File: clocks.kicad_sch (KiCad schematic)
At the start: 1 part, among them U10 Si5351C-B-GM

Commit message: Minor updates
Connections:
- net GND: now reaches U10.21 (GND)
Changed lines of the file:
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@@
 	(paper "A4")
 	(symbol
-		(lib_id "Oscillator:Si5351C-B-GM")
-		(at 85.09 87.63 0)
+		(lib_id "power:GND")
+		(at 115.57 92.71 0)
 		(unit 1)
 		(exclude_from_sim no)
@@
 		(on_board yes)
 		(dnp no)
+		(fields_autoplaced yes)
+		(property "Reference" "#PWR058"
+			(at 115.57 99.06 0)
+			(effects
+				(font
+					(size 1.27 1.27)
+				)
+				(hide yes)
+			)
+		)
+		(property "Value" "GND"
+			(at 115.57 97.79 0)
+			(effects
+				(font
+					(size 1.27 1.27)
+				)
+			)
+		)
+		(property "Footprint" ""
+			(at 115.57 92.71 0)
+			(effects
+				(font
+					(size 1.27 1.27)
+				)
+				(hide yes)
+			)
+		)
+		(property "Datasheet" ""
+			(at 115.57 92.71 0)
+			(effects
+				(font
+					(size 1.27 1.27)
+				)
+				(hide yes)
+			)
+		)
+		(property "Description" "Power symbol creates a global label with name \"GND\" , ground"
+			(at 115.57 92.71 0)
+			(effects
+				(font
+					(size 1.27 1.27)
+				)
+				(hide yes)
+			)
+		)
+		(pin "1"
+		)
+		(instances
+			(project ""
+				(path "/b16dfd04-6bfc-4d2d-ba2c-9a843d57dfb1/bef03a1a-2df5-41e5-bcca-109c5f92fdce"
+					(reference "#PWR058")
+					(unit 1)
+				)
+			)
+		)
+	)
+	(symbol
+		(lib_id "Oscillator:Si5351C-B-GM")
+		(at 115.57 69.85 0)
+		(unit 1)
+		(exclude_from_sim no)
+		(in_bom yes)
+		(on_board yes)
+		(dnp no)
+		(fields_autoplaced yes)
 		(property "Reference" "U10"
-			(at 87.2841 110.49 0)
+			(at 117.7641 92.71 0)
 			(effects
 				(font
@@
 		)
 		(property "Value" "Si5351C-B-GM"
-			(at 87.2841 113.03 0)
+			(at 117.7641 95.25 0)
 			(effects
 				(font
@@
 		)
 		(property "Footprint" "Package_DFN_QFN:QFN-20-1EP_4x4mm_P0.5mm_EP2.7x2.7mm"
-			(at 85.09 118.11 0)
+			(at 115.57 100.33 0)
 			(effects
 				(font
@@
 		)
 		(property "Datasheet" "https://www.silabs.com/documents/public/data-sheets/Si5351-B.pdf"
-			(at 85.09 87.63 0)
+			(at 115.57 69.85 0)
 			(effects
 				(font
@@
 		)
 		(property "Description" "I2C Programmable Any-Frequency CMOS Clock Generator, QFN-20"
-			(at 85.09 87.63 0)
+			(at 115.57 69.85 0)
 			(effects
 				(font
@@
 			)
 		)
-		(pin "2"
-		)
-		(pin "21"
-		)
-		(pin "8"
-		)
-		(pin "10"
-		)
-		(pin "1"
-		)
-		(pin "18"
-		)
-		(pin "19"
-		)
-		(pin "11"
-		)
-		(pin "17"
-		)
-		(pin "16"
+		(pin "20"
 		)
 		(pin "9"
@@
 		(pin "12"
 		)
+		(pin "18"
+		)
+		(pin "14"
+		)
+		(pin "16"
+		)
 		(pin "3"
+		)
+		(pin "15"
+		)
+		(pin "17"
+		)
+		(pin "4"
+		)
+		(pin "2"
+		)
+		(pin "10"
+		)
+		(pin "7"
+		)
+		(pin "19"
+		)
+		(pin "8"
+		)
+		(pin "21"
+		)
+		(pin "6"
+		)
+		(pin "1"
+		)
+		(pin "11"
+		)
+		(pin "13"
 		)
 		(pin "5"
 		)
-		(pin "4"
-		)
-		(pin "7"
-		)
-		(pin "6"
-		)
-		(pin "14"
-		)
-		(pin "15"
-		)
-		(pin "20"
-		)
-		(pin "13"
-		)
 		(instances
-			(project "albert"
+			(project ""
 				(path "/b16dfd04-6bfc-4d2d-ba2c-9a843d57dfb1/bef03a1a-2df5-41e5-bcca-109c5f92fdce"
 					(reference "U10")

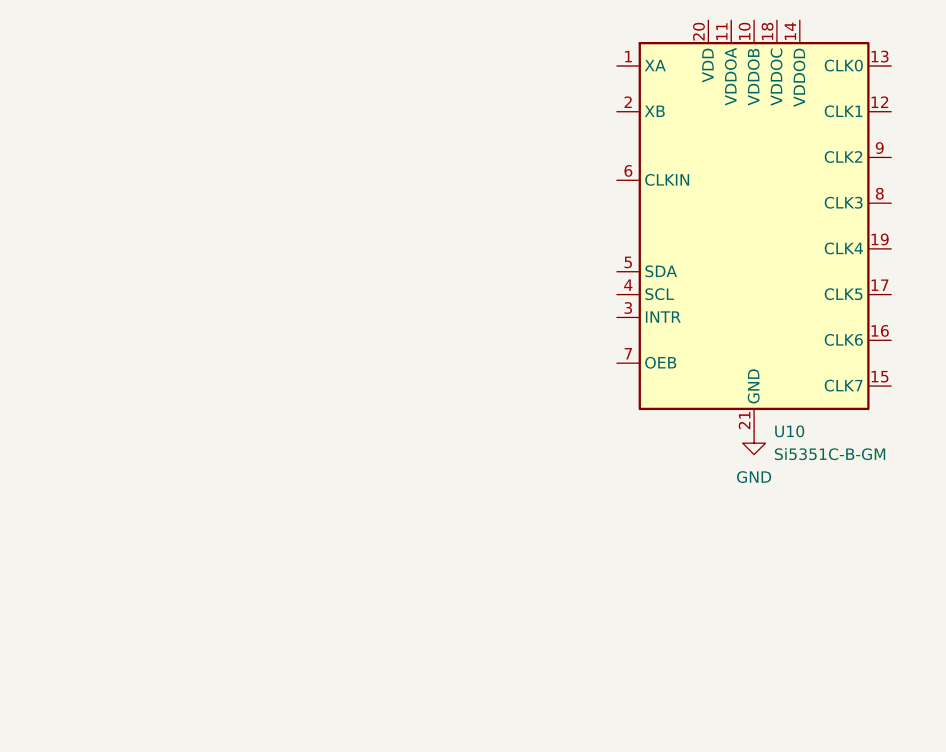
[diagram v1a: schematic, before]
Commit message: Added pMCU
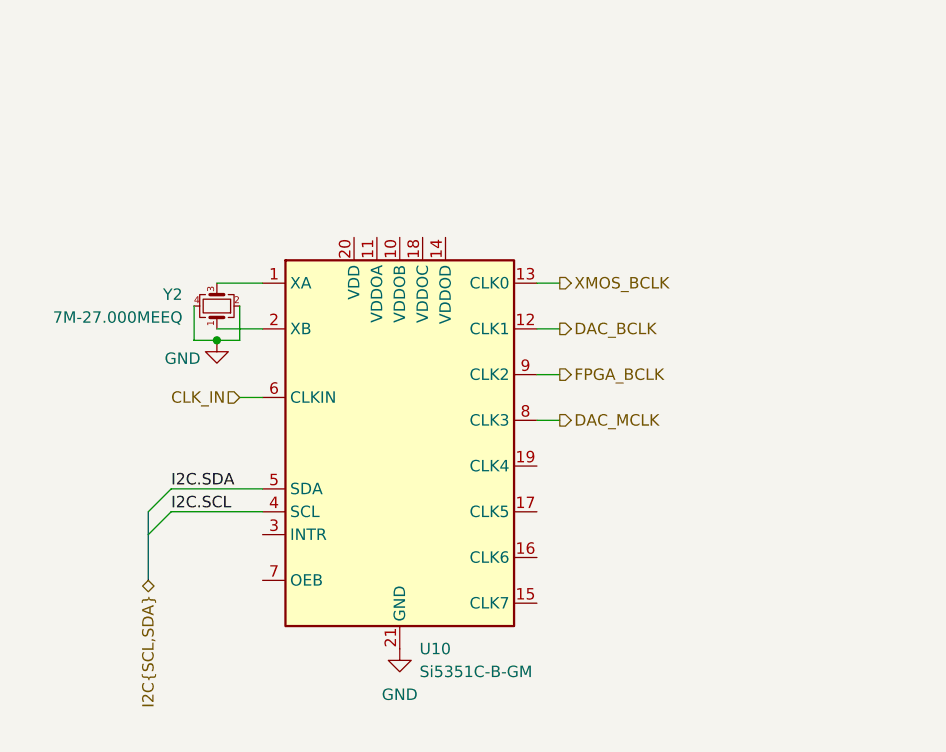
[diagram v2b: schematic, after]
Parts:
- added Y2: 7M-27.000MEEQ, symbol Device:Crystal_GND24_Small
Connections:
- net GND: now also Y2.2, Y2.4
- net at U10.1 (XA): now also Y2.3
- net DAC_BCLK: now reaches U10.12 (CLK1)
- net XMOS_BCLK: now reaches U10.13 (CLK0)
- net at U10.2 (XB): now also Y2.1
- net I2C.SCL: now reaches U10.4 (SCL)
- net I2C.SDA: now reaches U10.5 (SDA)
- net CLK_IN: now reaches U10.6 (CLKIN)
- net DAC_MCLK: now reaches U10.8 (CLK3)
- net FPGA_BCLK: now reaches U10.9 (CLK2)
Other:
- moved on the sheet: U10
